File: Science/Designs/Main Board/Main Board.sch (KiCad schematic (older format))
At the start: 51 parts

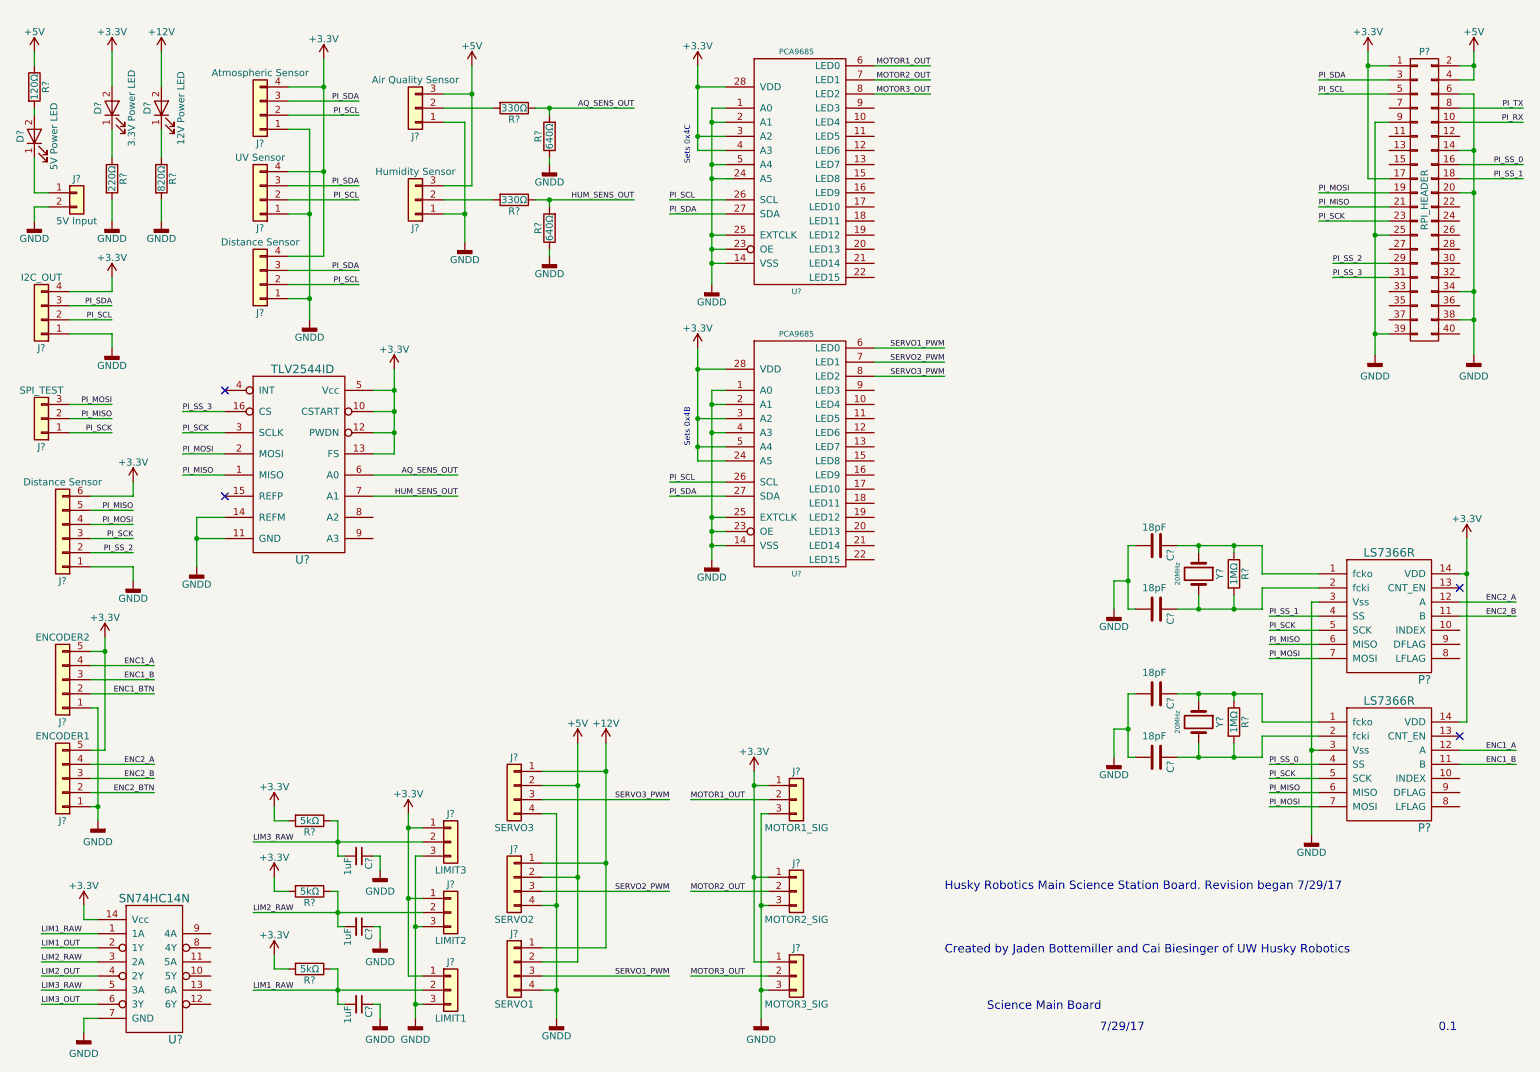
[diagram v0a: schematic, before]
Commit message: Added decoupling capacitors, started component associatons, added RGB LEDs
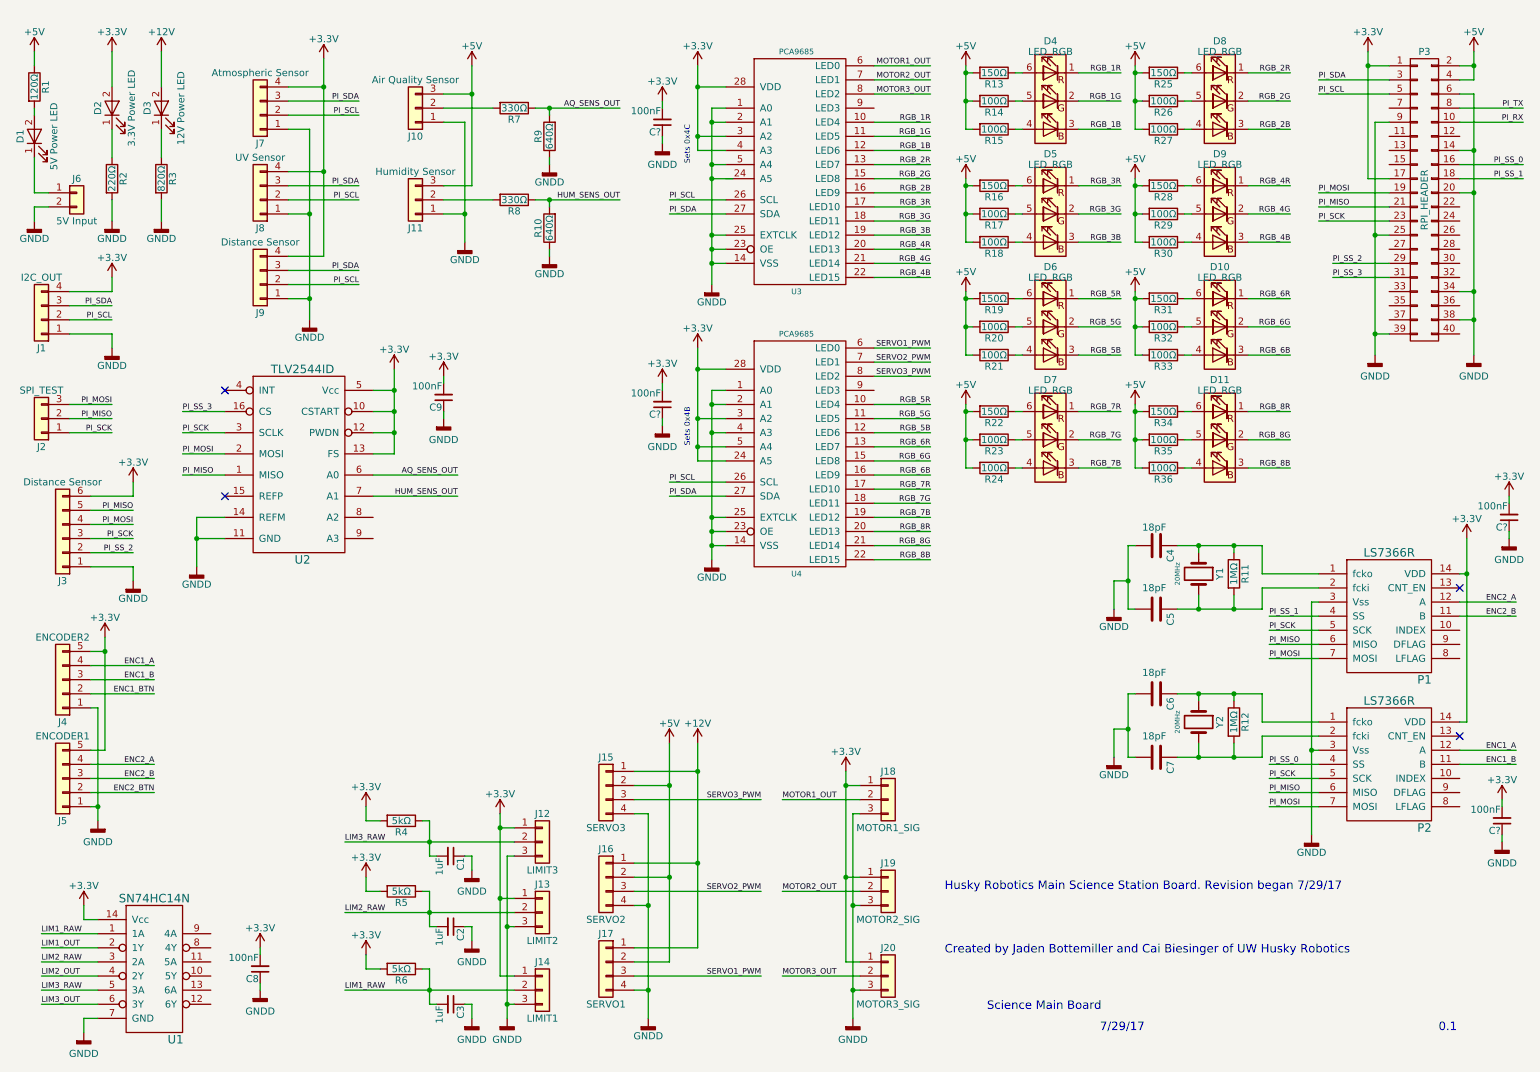
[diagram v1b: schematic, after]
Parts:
- added C8, C9, C? (x4): 100nF, Capacitors_SMD:C_1206_HandSoldering, symbol C_Small
- added D10, D11, D4, D5, D6, D7, D8, D9: LED_RGB, symbol LED_RGB
- added R13, R16, R19, R22, R25, R28, R31, R34: 150Ω, Resistors_SMD:R_1206_HandSoldering, symbol R
- added R14, R15, R17, R18, R20, R21, R23, R24, R26, R27, R29, R30, R32, R33, R35, R36: 100Ω, Resistors_SMD:R_1206_HandSoldering, symbol R
- C1, C2, C3, C4, C5, C6, C7: renamed from C?; footprint (none) -> Capacitors_SMD:C_1206_HandSoldering
- R1, R10, R11, R12, R2, R3, R4, R5, R6, R7, R8, R9: renamed from R?; footprint (none) -> Resistors_SMD:R_1206_HandSoldering
- gave numbers to parts that had none: 32
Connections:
- net +3V3: now also C8.2, C9.2, C?.2, C?.2, C?.2, C?.2
- net +5V: now also R13.2, R14.2, R15.2, R16.2, R17.2, R18.2, R19.2, R20.2, R21.2, R22.2, R23.2, R24.2, R25.2, R26.2, R27.2, R28.2, R29.2, R30.2, R31.2, R32.2, R33.2, R34.2, R35.2, R36.2
- net GNDD: now also C8.1, C9.1, C?.1, C?.1, C?.1, C?.1
- net RGB_5R: now reaches U4.10 (LED4)
- net RGB_5R: now also D6.1 (RK)
- net RGB_5G: now reaches U4.11 (LED5)
- net RGB_5G: now also D6.2 (GK)
- net RGB_5B: now reaches U4.12 (LED6)
- net RGB_5B: now also D6.3 (BK)
- net RGB_6R: now reaches U4.13 (LED7)
- net RGB_6R: now also D10.1 (RK)
- net RGB_6G: now reaches U4.15 (LED8)
- net RGB_6G: now also D10.2 (GK)
- net RGB_6B: now reaches U4.16 (LED9)
- net RGB_6B: now also D10.3 (BK)
- net RGB_7R: now reaches U4.17 (LED10)
- net RGB_7R: now also D7.1 (RK)
- net RGB_7G: now reaches U4.18 (LED11)
- net RGB_7G: now also D7.2 (GK)
- net RGB_7B: now reaches U4.19 (LED12)
- net RGB_7B: now also D7.3 (BK)
- net RGB_8R: now reaches U4.20 (LED13)
- net RGB_8R: now also D11.1 (RK)
- net RGB_8G: now reaches U4.21 (LED14)
- net RGB_8G: now also D11.2 (GK)
- net RGB_8B: now reaches U4.22 (LED15)
- net RGB_8B: now also D11.3 (BK)
- net RGB_1R: now reaches U3.10 (LED4)
- net RGB_1R: now also D4.1 (RK)
- net RGB_1G: now reaches U3.11 (LED5)
- net RGB_1G: now also D4.2 (GK)
- net RGB_1B: now reaches U3.12 (LED6)
- net RGB_1B: now also D4.3 (BK)
- net RGB_2R: now reaches U3.13 (LED7)
- net RGB_2R: now also D8.1 (RK)
- net RGB_2G: now reaches U3.15 (LED8)
- net RGB_2G: now also D8.2 (GK)
- net RGB_2B: now reaches U3.16 (LED9)
- net RGB_2B: now also D8.3 (BK)
- net RGB_3R: now reaches U3.17 (LED10)
- net RGB_3R: now also D5.1 (RK)
- net RGB_3G: now reaches U3.18 (LED11)
- net RGB_3G: now also D5.2 (GK)
- net RGB_3B: now reaches U3.19 (LED12)
- net RGB_3B: now also D5.3 (BK)
- net RGB_4R: now reaches U3.20 (LED13)
- net RGB_4R: now also D9.1 (RK)
- net RGB_4G: now reaches U3.21 (LED14)
- net RGB_4G: now also D9.2 (GK)
- net RGB_4B: now reaches U3.22 (LED15)
- net RGB_4B: now also D9.3 (BK)
- new net: D4.4 (BA), R15.1
- new net: D4.5 (GA), R14.1
- new net: D4.6 (RA), R13.1
- new net: D5.4 (BA), R18.1
- new net: D5.5 (GA), R17.1
- new net: D5.6 (RA), R16.1
- new net: D6.4 (BA), R21.1
- new net: D6.5 (GA), R20.1
- new net: D6.6 (RA), R19.1
- new net: D7.4 (BA), R24.1
- new net: D7.5 (GA), R23.1
- new net: D7.6 (RA), R22.1
- new net: D8.4 (BA), R27.1
- new net: D8.5 (GA), R26.1
- new net: D8.6 (RA), R25.1
- new net: D9.4 (BA), R30.1
- new net: D9.5 (GA), R29.1
- new net: D9.6 (RA), R28.1
- new net: D10.4 (BA), R33.1
- new net: D10.5 (GA), R32.1
- new net: D10.6 (RA), R31.1
- new net: D11.4 (BA), R36.1
- new net: D11.5 (GA), R35.1
- new net: D11.6 (RA), R34.1
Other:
- moved on the sheet: C1, C2, C3, J12, J13, J14, J15, J16, J17, J18, J19, J20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

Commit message: Cleaning up schematic, adding I2C test connector
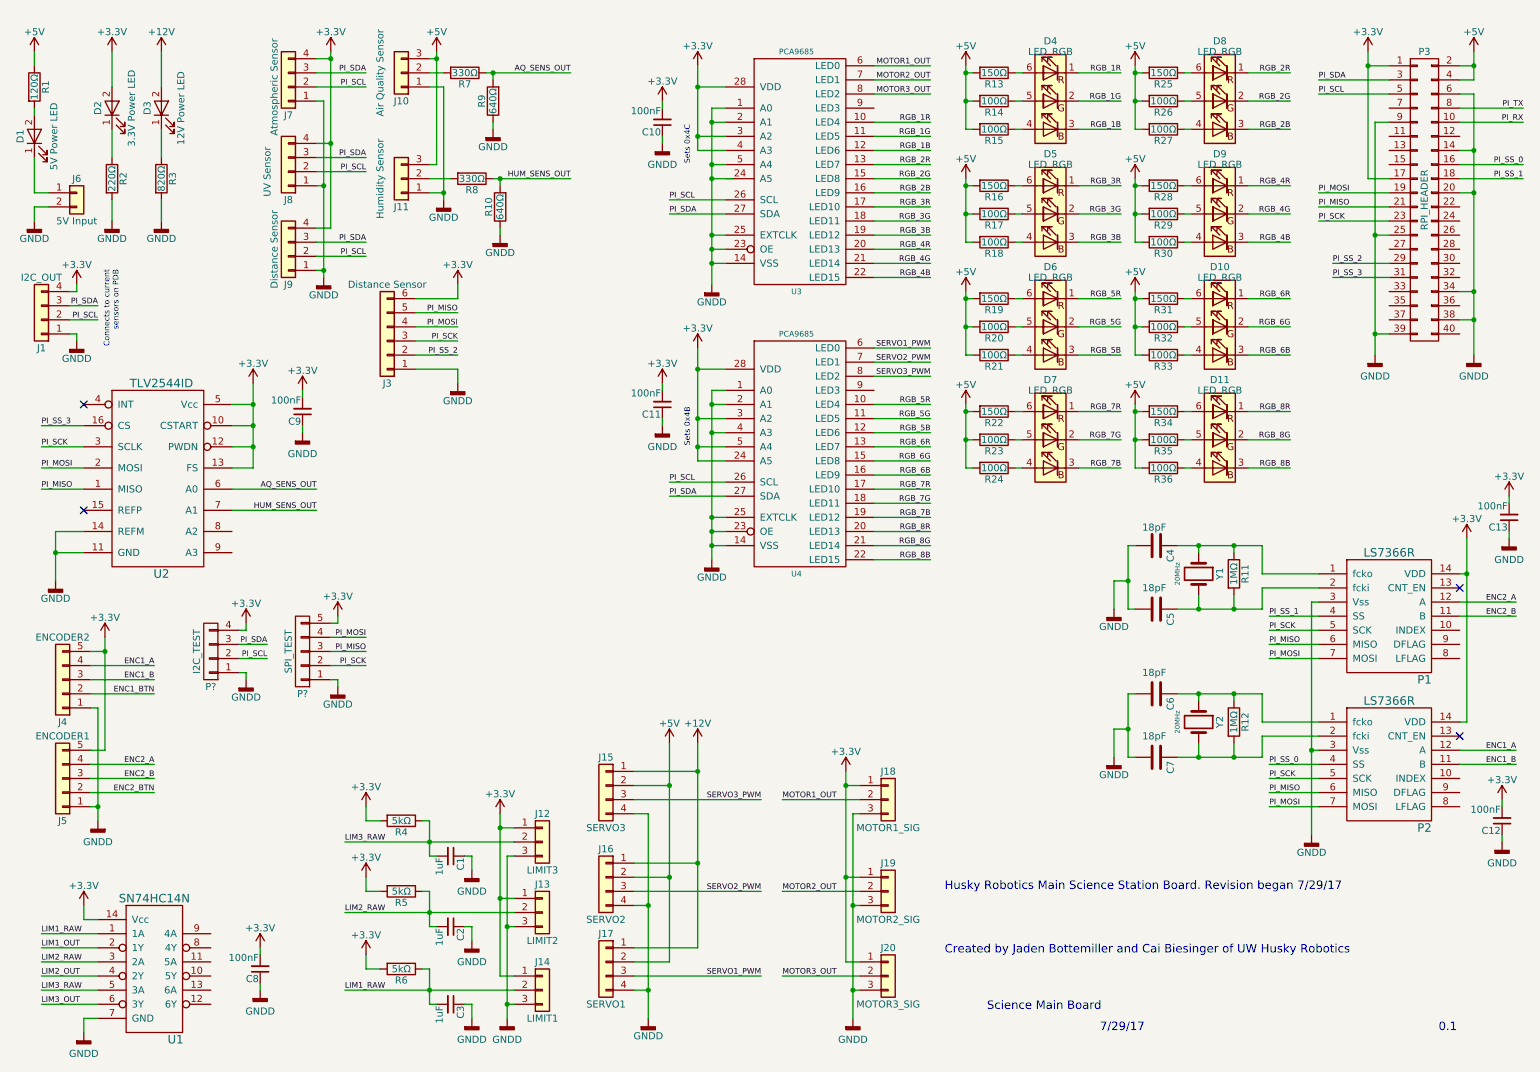
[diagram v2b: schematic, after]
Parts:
- removed J2: SPI_TEST, symbol Conn_01x03
- added P?: I2C_TEST, symbol CONN_01X04
- added P?: SPI_TEST, symbol CONN_01X05
- gave numbers to parts that had none: 4
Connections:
- net +3V3: now also P?.4 (P4), P?.5 (P5)
- net GNDD: now also P?.1 (P1), P?.1 (P1)
- net PI_MISO: now also P?.3 (P3)
- net PI_MOSI: now also P?.4 (P4)
- net PI_SCK: now also P?.2 (P2)
- net PI_SCL: now also P?.2 (P2)
- net PI_SDA: now also P?.3 (P3)
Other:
- note added: "Connects to current\nsensors on PDB"
- moved on the sheet: C9, J10, J11, J3, J7, J8, J9, R10, R7, R8, R9, U2

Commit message: Fixing various board issues
Decoupling caps, power connector, sensor connectors, power LEDs, etc.
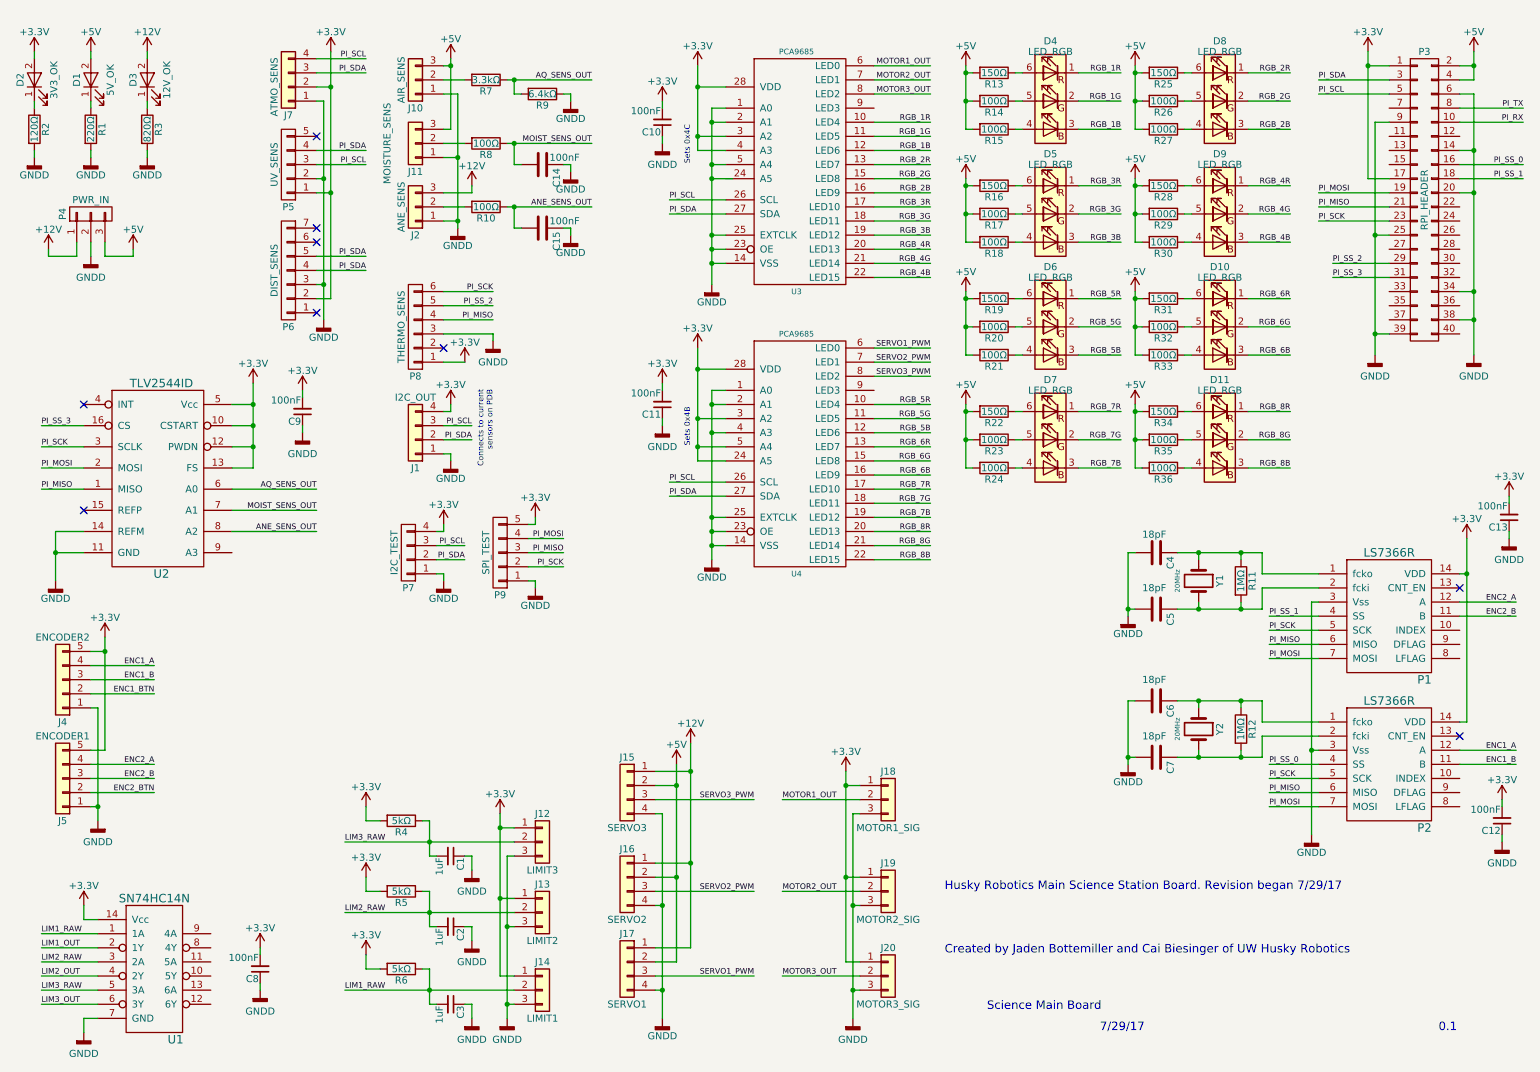
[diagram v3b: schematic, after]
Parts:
- removed J3: Distance Sensor, symbol Conn_01x06
- removed J6: 5V Input, symbol Conn_01x02
- removed J8: UV Sensor, symbol Conn_01x04
- removed J9: Distance Sensor, symbol Conn_01x04
- added C14, C15: 100nF, symbol C
- added J2: ANE_SENS, symbol Conn_01x03
- added P4: PWR_IN, symbol CONN_01X03
- added P5: UV_SENS, symbol CONN_01X05
- added P6: DIST_SENS, symbol CONN_01X07
- added P8: THERMO_SENS, symbol CONN_01X06
- D1: value 5V Power LED -> 5V_OK
- D2: value 3.3V Power LED -> 3V3_OK
- D3: value 12V Power LED -> 12V_OK
- J10: value Air Quality Sensor -> AIR_SENS
- J11: value Humidity Sensor -> MOISTURE_SENS
- J7: value Atmospheric Sensor -> ATMO_SENS
- R1: value 120Ω -> 220Ω
- R10: value 640Ω -> 100Ω
- R2: value 220Ω -> 120Ω
- R7: value 330Ω -> 3.3kΩ
- R8: value 330Ω -> 100Ω
- R9: value 640Ω -> 6.4kΩ
- gave numbers to parts that had none: 2
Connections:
- net +12V: now also J2.3 (Pin_3), P4.1 (P1)
- net +3V3: now also J7.2 (Pin_2), P5.1 (P1), P6.2 (P2), P8.1 (P1); no longer J7.4 (Pin_4)
- net +5V: now also D1.2 (A), P4.3 (P3); no longer R1.1
- net GNDD: now also R1.2, C14.1, C15.1, J2.1 (Pin_1), P4.2 (P2), P5.2 (P2), P6.3 (P3), P8.3 (P3); no longer R10.1
- net PI_MISO: now also P8.4 (P4)
- net PI_SCK: now also P8.6 (P6)
- net PI_SCL: now also J1.3 (Pin_3), J7.4 (Pin_4), P7.3 (P3), P5.3 (P3); no longer J1.2 (Pin_2), J7.2 (Pin_2), P7.2 (P2)
- net PI_SDA: now also J1.2 (Pin_2), P7.2 (P2), P5.4 (P4), P6.4 (P4), P6.5 (P5); no longer J1.3 (Pin_3), P7.3 (P3)
- net PI_SS_2: now also P8.5 (P5)
- net at D1.1 (K): now also R1.1
- net ANE_SENS_OUT: now reaches U2.8 (A2)
- net ANE_SENS_OUT: now also R10.1, C15.2
- net HUM_SENS_OUT renamed MOIST_SENS_OUT
- net MOIST_SENS_OUT: now also C14.2; no longer R10.2
- new net: J2.2 (Pin_2), R10.2
- no-connect marks 4 -> 9
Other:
- moved on the sheet: C4, C6, D1, D2, D3, J1, J10, J11, J15, J16, J17, P7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

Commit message: Fixed issues
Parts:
- added R?: 10kΩ, symbol R
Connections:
- net +3V3: now also R?.1
- net GNDD: now also P3.30 (P30), U3.24 (A5); no longer P3.38 (P38)
- net at P1.13 (CNT_EN): now also R?.2
- no-connect marks 9 -> 11
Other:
- moved on the sheet: C13

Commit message: Added missing pullup
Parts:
- added R?: 10kΩ, symbol R
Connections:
- net +3V3: now also R?.1
- net at P2.13 (CNT_EN): now also R?.2
- no-connect marks 11 -> 10
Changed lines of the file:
@@
 Text Label 3700 3350 2    40   ~ 0
 PI_SCL
-NoConn ~ 10700 5550
 Text Label 9700 1900 0    40   ~ 0
 PI_SCK
@@
 	9700 4400 9300 4400
 Wire Wire Line
-	9300 4250 9300 4400
-Wire Wire Line
-	8700 4250 9300 4250
+	9300 4400 9300 4250
+Wire Wire Line
+	9300 4250 8700 4250
 Wire Wire Line
 	9700 4500 9300 4500
 Wire Wire Line
-	9300 4650 9300 4500
-Wire Wire Line
-	8700 4650 9300 4650
+	9300 4500 9300 4650
+Wire Wire Line
+	9300 4650 8700 4650
 Wire Wire Line
 	9150 4300 9150 4250
@@
 	10700 2200 10800 2200
 Connection ~ 10800 2200
+$Comp
+L R R?
+U 1 1 5A5F2910
+P 10950 5350
+F 0 "R?" V 11030 5350 50  0000 C CNN
+F 1 "10kΩ" V 10950 5350 50  0000 C CNN
+F 2 "" V 10880 5350 50  0000 C CNN
+F 3 "" H 10950 5350 50  0000 C CNN
+	1    10950 5350
+	1    0    0    -1
+$EndComp
+Wire Wire Line
+	10950 5200 10950 5150
+Wire Wire Line
+	10950 5150 10750 5150
+Connection ~ 10750 5150
+Wire Wire Line
+	10700 5550 10950 5550
+Wire Wire Line
+	10950 5550 10950 5500
 $EndSCHEMATC
